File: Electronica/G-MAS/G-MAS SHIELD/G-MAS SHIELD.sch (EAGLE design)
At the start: 28 parts, among them T1-V1 2N2222, T1-V2 2N2222, T1-V3 2N2222, T1-V4 2N2222, T1-V5 2N2222

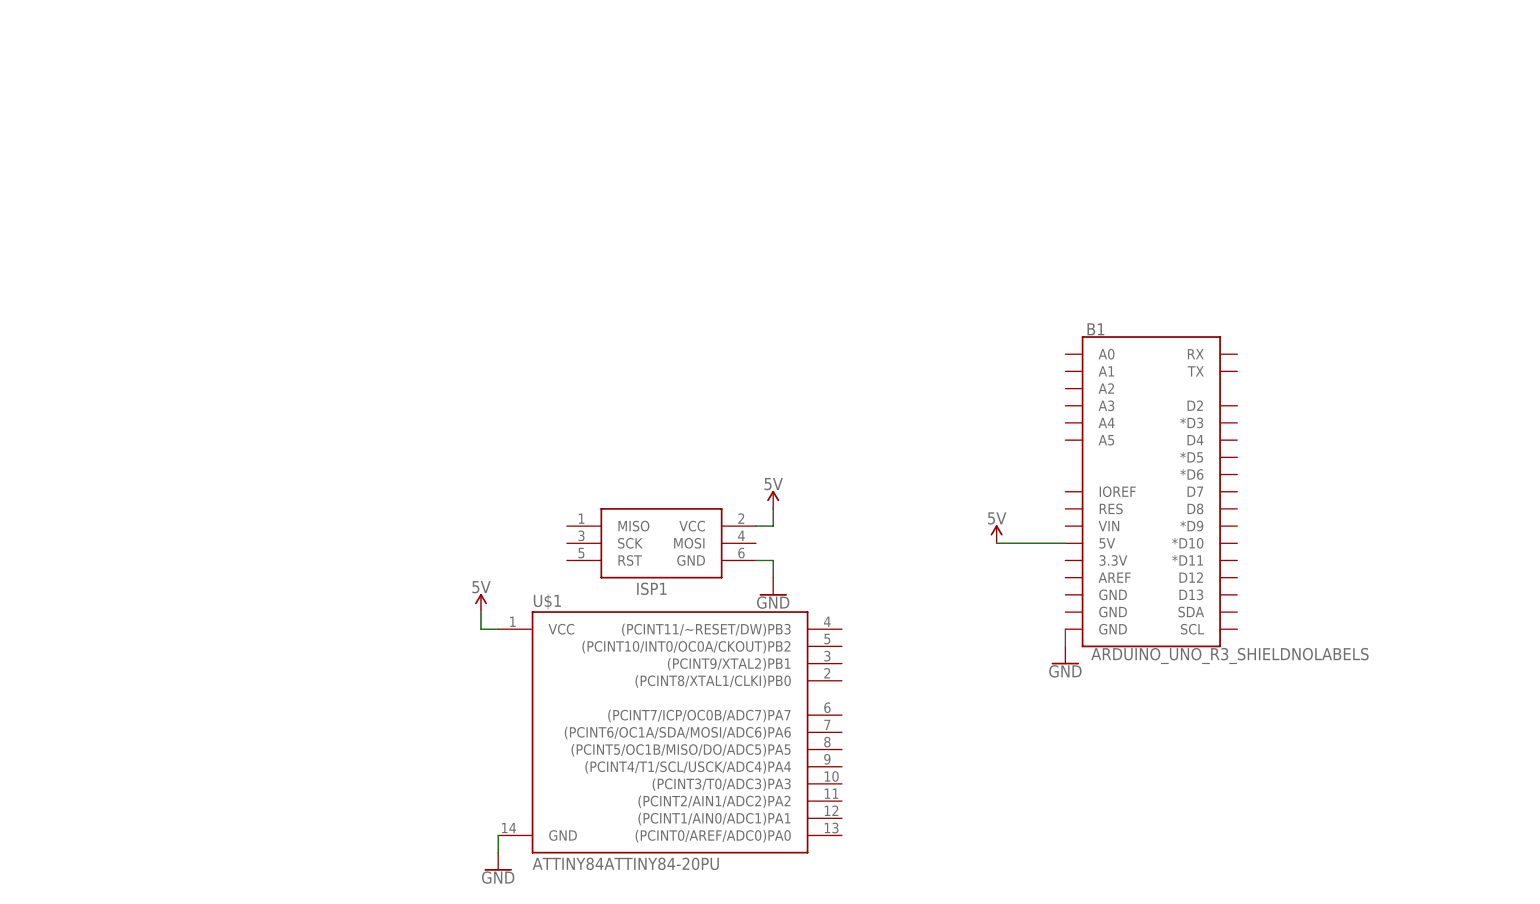
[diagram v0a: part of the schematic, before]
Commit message: Vibration Sensor Module
Incorpotation of the first version of the sensor module, beta, using attiny84.
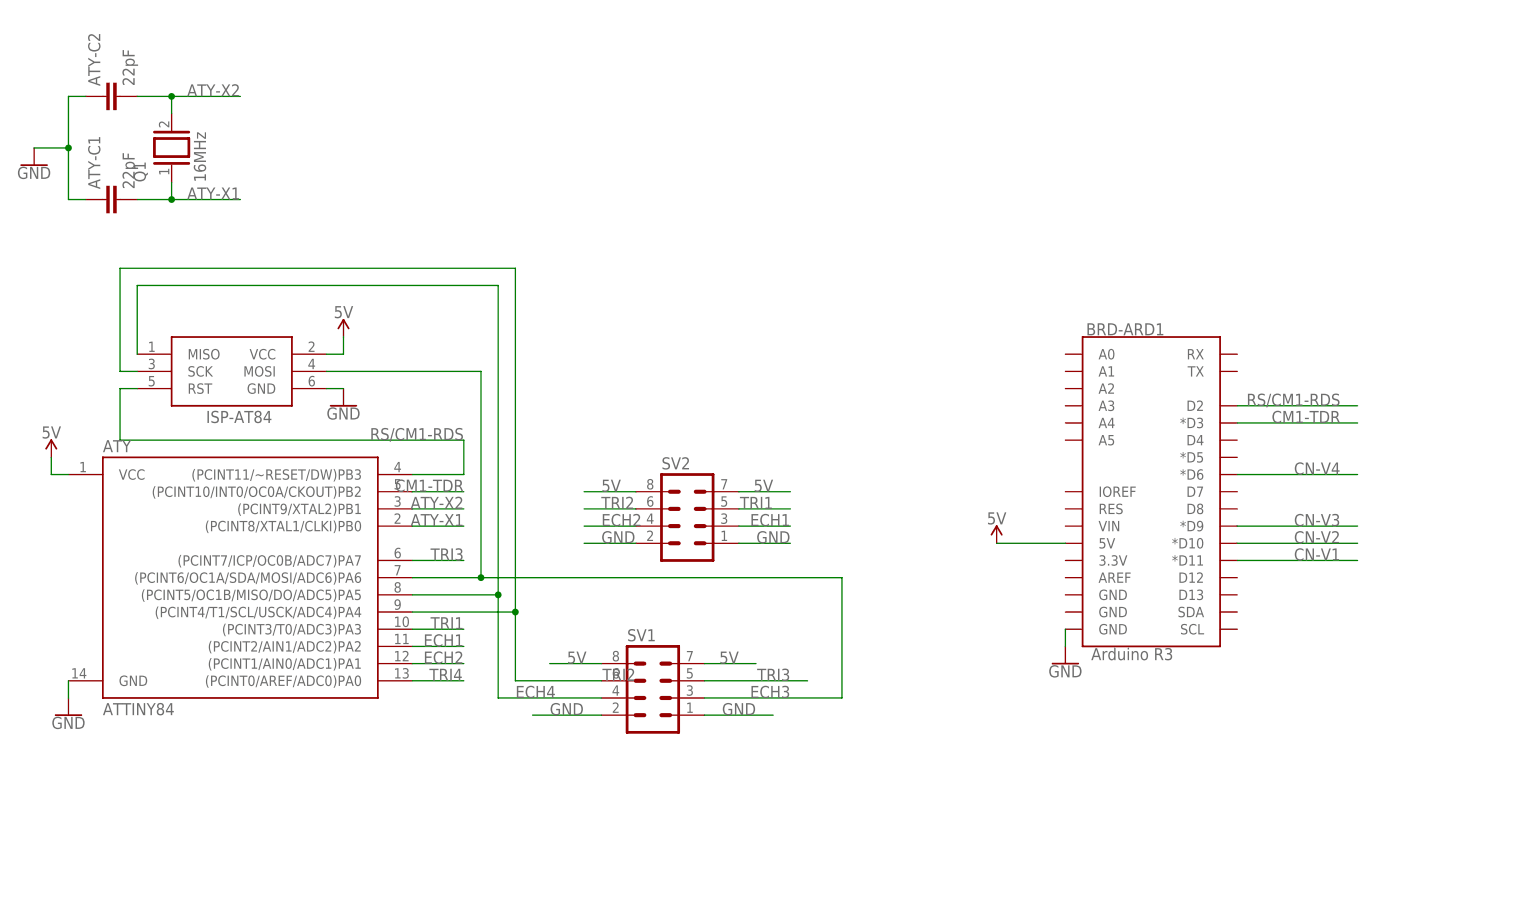
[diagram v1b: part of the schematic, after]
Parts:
- removed ISP1: AVRISP-6, adafruit:AVRISP-6
- removed U$1: ATTINY84ATTINY84-20PU, SparkFun-IC-Microcontroller:ATTINY84ATTINY84-20PU
- added ATY: ATTINY84, SparkFun-IC-Microcontroller:ATTINY84ATTINY84-20PU
- added ATY-C1, ATY-C2: 22pF, SparkFun-Capacitors:0.1UF-KIT-EZ-50V-20%
- added ISP-AT84: AVRISP-6, adafruit:AVRISP-6
- added Q1: 16MHz, special:XTAL/S
- added SV1, SV2: (no value), con-lstb:MA04-2
- BRD-ARD1: value ARDUINO_UNO_R3_SHIELDNOLABELS -> Arduino R3
- T1-V1, T1-V2, T1-V3, T1-V4, T1-V5: device transistor:2N2222 -> adafruit:2N2222
- renumbered B1 to BRD-ARD1
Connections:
- new net ATY-X1: ATY-C1.2, ATY.(PCINT8/XTAL1/CLKI)PB0, Q1.1
- new net ATY-X2: ATY-C2.2, ATY.(PCINT9/XTAL2)PB1, Q1.2
- new net CM1-TDR: ATY.(PCINT10/INT0/OC0A/CKOUT)PB2, BRD-ARD1.*D3
- new net ECH1: ATY.(PCINT2/AIN1/ADC2)PA2, SV2.3
- new net ECH2: ATY.(PCINT1/AIN0/ADC1)PA1, SV2.4
- new net ECH3: ATY.(PCINT6/OC1A/SDA/MOSI/ADC6)PA6, ISP-AT84.MOSI, SV1.3
- new net ECH4: ATY.(PCINT5/OC1B/MISO/DO/ADC5)PA5, ISP-AT84.MISO, SV1.4
- new net RS/CM1-RDS: ATY.(PCINT11/~RESET/DW)PB3, BRD-ARD1.D2, ISP-AT84.RST
- new net TRI1: ATY.(PCINT3/T0/ADC3)PA3, SV2.5
- new net TRI2: ATY.(PCINT0/AREF/ADC0)PA0, SV2.6
- new net TRI3: ATY.(PCINT7/ICP/OC0B/ADC7)PA7, SV1.5
- new net TRI4: ATY.(PCINT4/T1/SCL/USCK/ADC4)PA4, ISP-AT84.SCK, SV1.6
- net 5V: now also ATY.VCC, ISP-AT84.VCC, SV1.7, SV1.8, SV2.7, SV2.8; no longer ISP1.VCC, U$1.VCC
- net CN-V1: now also BRD-ARD1.*D11
- net CN-V2: now also BRD-ARD1.*D10
- net CN-V3: now also BRD-ARD1.*D9
- net CN-V4: now also BRD-ARD1.*D6
- net GND: now also ATY-C1.1, ATY-C2.1, ATY.GND, ISP-AT84.GND, SV1.1, SV1.2, SV2.1, SV2.2; no longer ISP1.GND, U$1.GND

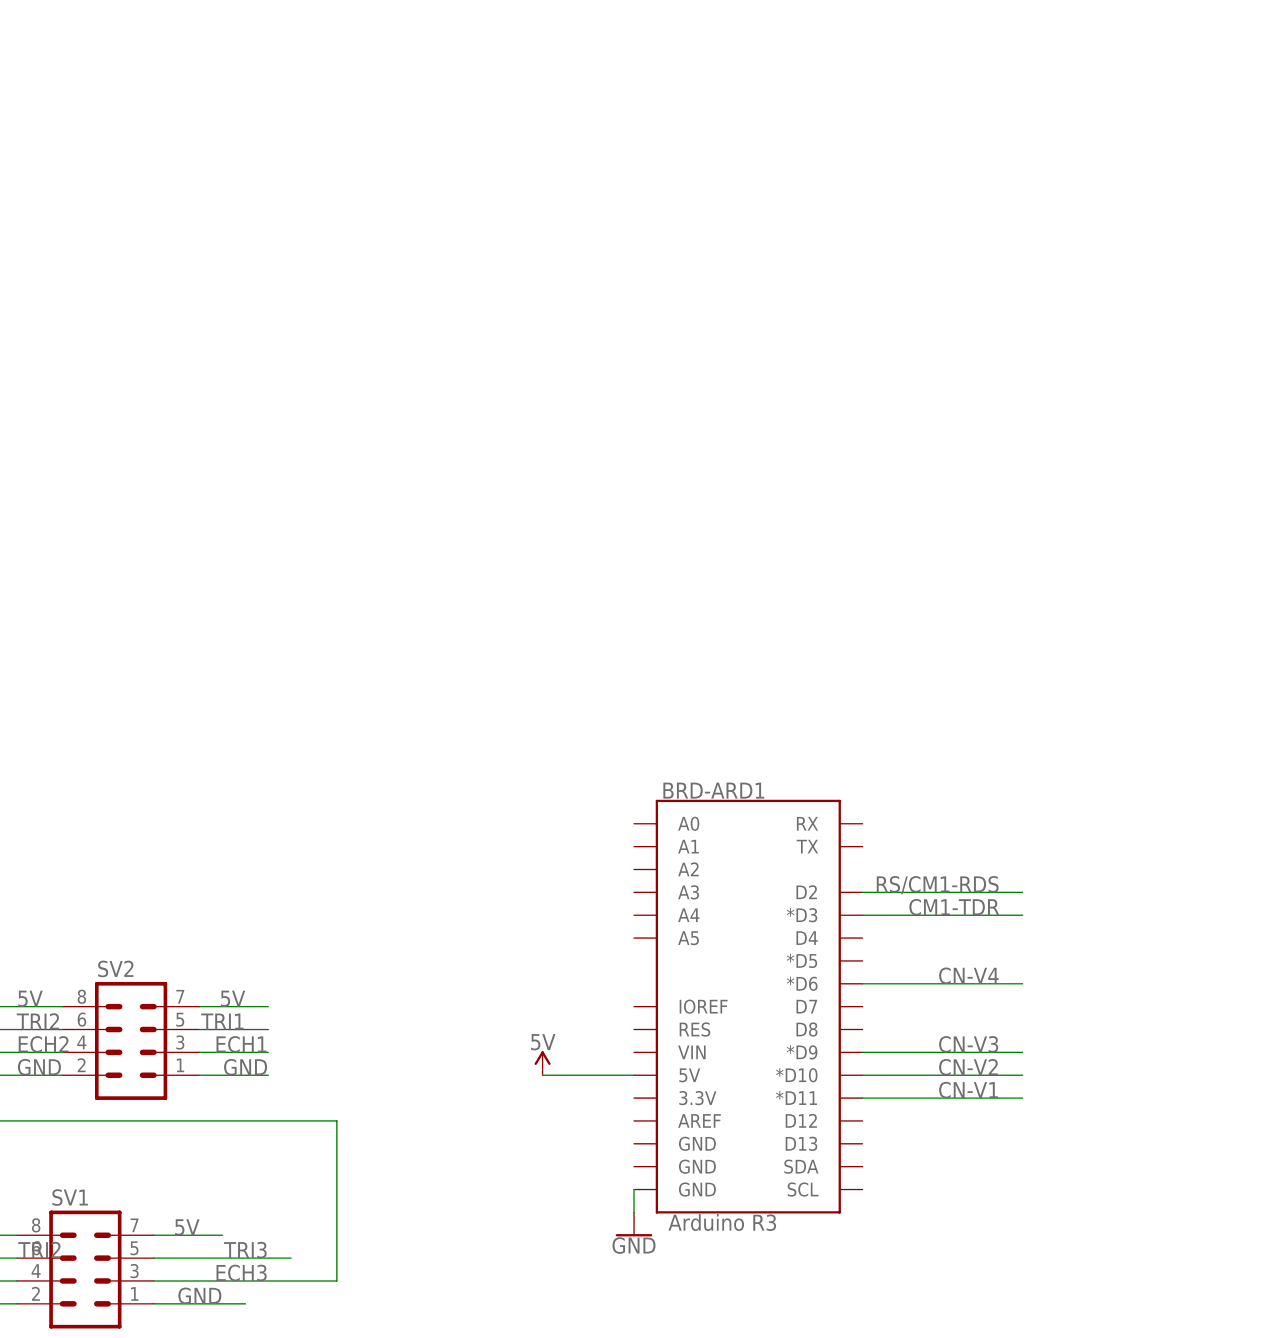
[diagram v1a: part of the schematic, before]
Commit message: V1
Incorporacion de MicroSD
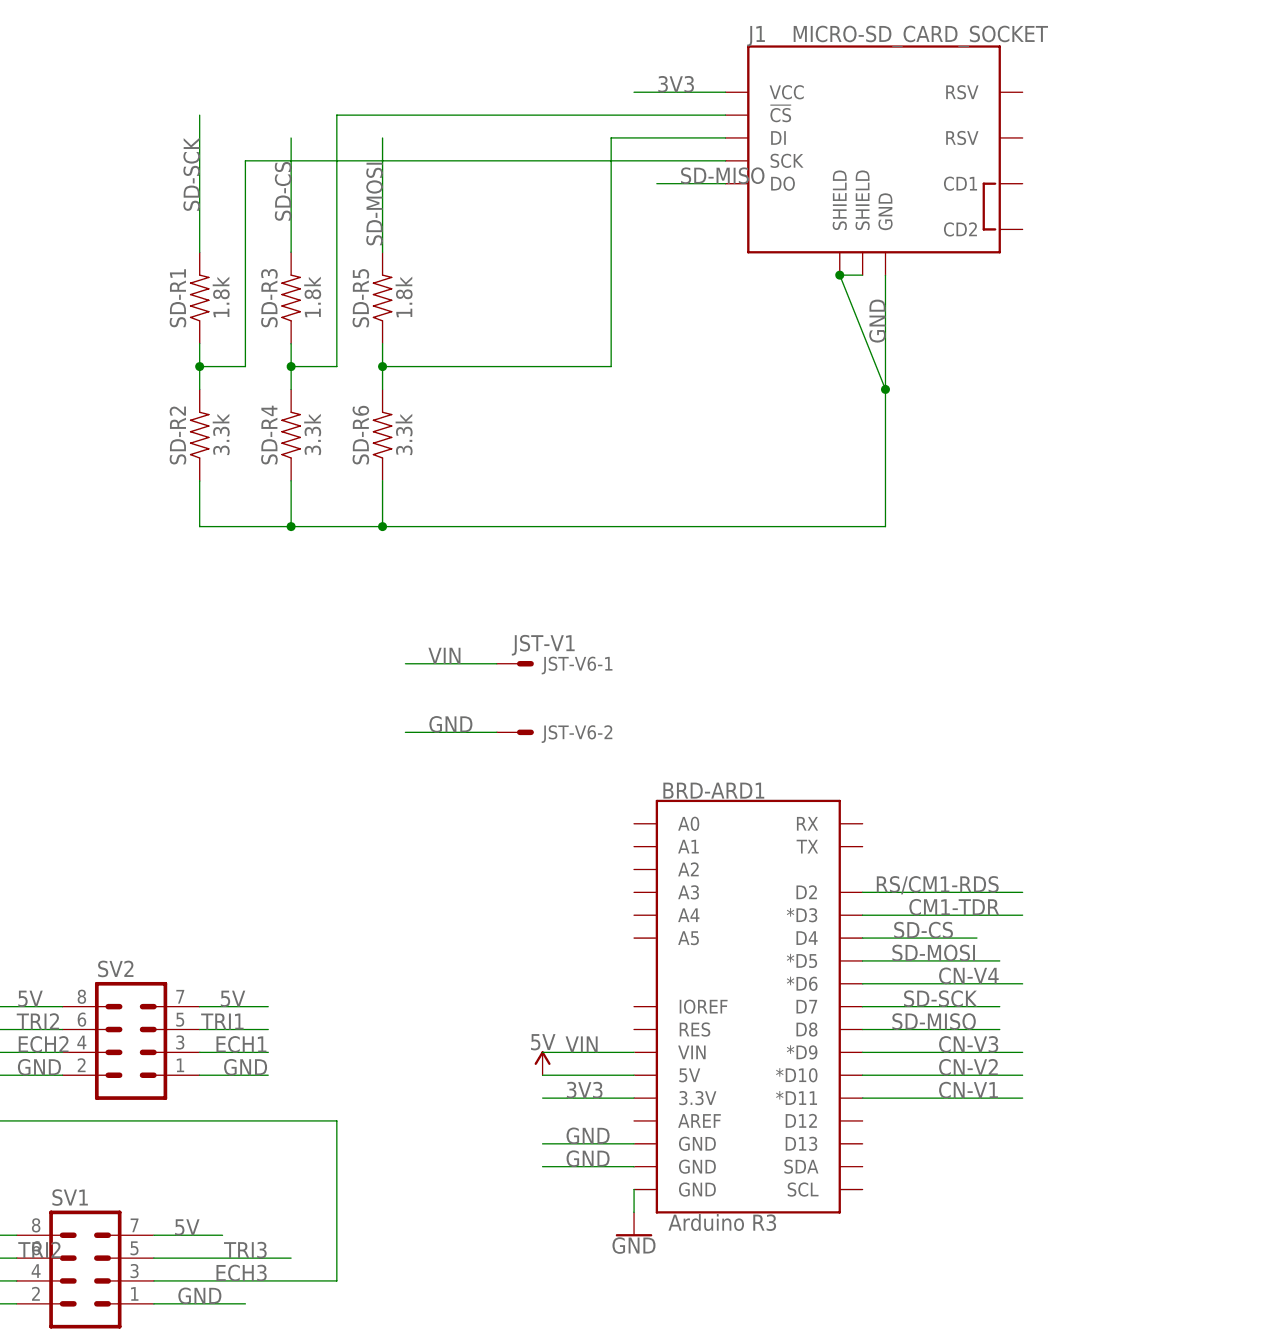
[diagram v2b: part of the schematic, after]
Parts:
- added J1: MICRO-SD_CARD_SOCKET, SparkFun-Connectors:MICRO-SD_CARD_SOCKET
- added JST-V6: JST-V1, Rembrandt Electronics - JST XH Connectors v1-0:JST-XH-02-PIN-LONG-PAD
- added SD-R1, SD-R3, SD-R5: 1.8k, SparkFun-Resistors:1.8KOHM-0603-1/10W-1%
- added SD-R2, SD-R4, SD-R6: 3.3k, SparkFun-Resistors:3.3KOHM-0603-1/10W-1%
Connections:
- new net 3V3: BRD-ARD1.3.3V, J1.VCC
- new net N$11: J1.SCK, SD-R1.1, SD-R2.2
- new net N$12: J1.!CS, SD-R3.1, SD-R4.2
- new net N$13: J1.DI, SD-R5.1, SD-R6.2
- new net SD-CS: BRD-ARD1.D4, SD-R3.2
- new net SD-MISO: BRD-ARD1.D8, J1.DO
- new net SD-MOSI: BRD-ARD1.*D5, SD-R5.2
- new net SD-SCK: BRD-ARD1.D7, SD-R1.2
- new net VIN: BRD-ARD1.VIN, JST-V6-1.S
- net GND: now also BRD-ARD1.GND@1, BRD-ARD1.GND@2, J1.GND, J1.SHIELD@1, J1.SHIELD@3, JST-V6-2.S, SD-R2.1, SD-R4.1, SD-R6.1
